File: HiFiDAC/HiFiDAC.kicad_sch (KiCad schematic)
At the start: 16 parts, among them J1 SE, J2 LDIFF, J3 RDIFF, J4 5V, J5 +-15V, U1 KC2520K24.5760

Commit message: HiFiDAC v2 progress
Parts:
- removed C16: 0.1µF C0G, BW_PassiveMechanical:C_0704_1810Metric, symbol Device:C_Small
- removed C2: 1µF 25V, Capacitor_SMD:C_0603_1608Metric, symbol Device:C
- added C1: 10µF 25V, Capacitor_SMD:C_0805_2012Metric, symbol Device:C_Small
- added C10, C11: 0.1µF, Capacitor_SMD:C_0603_1608Metric, symbol Device:C_Small
- added C2, C4, C5, C6: 1µF 25V, Capacitor_SMD:C_0603_1608Metric, symbol Device:C_Small
- added C9: 4.7µF, Capacitor_SMD:C_0603_1608Metric, symbol Device:C_Small
- added FB1: MPZ1608B471ATA00, Inductor_SMD:L_0603_1608Metric, symbol Device:FerriteBead
- added J2: I2S, BW_Connectors:Amphenol_MINITEK_0.8_6P_V, symbol Connector:Conn_01x06_Pin
- added J5: SWD, Connector_PinSocket_1.27mm:PinSocket_1x05_P1.27mm_Vertical_SMD_Pin1Right, symbol Connector:Conn_01x05_Socket
- added J6: I2C, BW_Connectors:Amphenol_MINITEK_0.8_4P_V, symbol Connector:Conn_01x04_Pin
- added R1: 2.2Ω, Resistor_SMD:R_0603_1608Metric, symbol Device:R_US
- added R4, R5: 27Ω, Resistor_SMD:R_0603_1608Metric, symbol Device:R_US
- added R6: 10kΩ, Resistor_SMD:R_0603_1608Metric, symbol Device:R_US
- added TP1: DEBUG_UART_TX, BW_PassiveMechanical:TP_0603_1608Metric_Fused, symbol Connector:TestPoint_Small
- added TP2: I2C_~{INT}, BW_PassiveMechanical:TP_0603_1608Metric_Fused, symbol Connector:TestPoint_Small
- added TP3: I2C_SDA, BW_PassiveMechanical:TP_0603_1608Metric_Fused, symbol Connector:TestPoint_Small
- added TP4: DEBUG_UART_RX, BW_PassiveMechanical:TP_0603_1608Metric_Fused, symbol Connector:TestPoint_Small
- added TP5: I2C_SCL, BW_PassiveMechanical:TP_0603_1608Metric_Fused, symbol Connector:TestPoint_Small
- added U2: ES9039Q2M, BW_Active:QFN-32-1EP_5x5mm_P0.5mm_EP3.2x3.2mm, symbol BW_Active:ES9039Q2M
- added U3: STM32C031K6Ux, Package_DFN_QFN:QFN-32-1EP_5x5mm_P0.5mm_EP3.45x3.45mm, symbol MCU_ST_STM32C0:STM32C031K6Ux
- C12: renamed from C14; value 47µF 20V -> 100µF 25V; footprint Capacitor_SMD:CP_Elec_5x5.8 -> Capacitor_SMD:CP_Elec_6.3x5.9
- C13: renamed from C4; value 100µF 10V 450mΩ -> 100µF 10V; footprint Capacitor_SMD:CP_Elec_6.3x7.7 -> Capacitor_THT:CP_Radial_D6.3mm_P2.50mm
- C14: renamed from C17; value 47µF 20V -> 100µF 25V; footprint Capacitor_SMD:CP_Elec_5x5.8 -> Capacitor_SMD:CP_Elec_6.3x5.9
- C3: value 0.1µF C0G -> 1µF 25V; footprint BW_PassiveMechanical:C_0704_1810Metric -> Capacitor_SMD:C_0603_1608Metric
- J3: renamed from J2; value LDIFF -> DIFF_1
- J4: renamed from J3; value RDIFF -> DIFF_2
- R3: value 0Ω -> 10Ω
- renumbered C12 to C7, C13 to C8, J4 to J7, J5 to J8, R4 to R2
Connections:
- net +3.3VD: now also C10.2, C9.2, FB1.1, J5.1 (Pin_1), R6.1, U3.4 (VDD)
- net GND: now also C10.1, C11.2, C2.2, C4.2, C5.2, C6.2, C9.1, J2.6 (Pin_6), J5.3 (Pin_3), J6.4 (Pin_4), R1.1, U2.11 (GND), U2.17 (RT1), U2.30 (GND), U2.33 (EP), U2.4 (AGND_DAC1), U2.5 (AGND_DAC2), U3.33 (VSS), U3.5 (VSS)
- net at R2.2, U1.3 (CLK): now also U2.32 (MCLK); no longer R3.1
- net at R3.2: now also U2.12 (DATA_CLK)
- net +3.3V: no longer names the net of C3.1
- net +3.3V: now also U2.9 (DVDD)
- net Digital Interface/SCK: no longer names the net of R2.1
- net Digital Interface/SCK: now also J2.5 (Pin_5)
- net I-V Stage/VL+ renamed I-V Stage/V1+
- net I-V Stage/VL- renamed I-V Stage/V1-
- net I-V Stage/VR+ renamed I-V Stage/V2+
- net I-V Stage/VR- renamed I-V Stage/V2-
- new net: J6.2 (Pin_2), TP3.1, U3.31 (PB7)
- new net: C1.1, C2.1, FB1.2, U2.10 (AVDD), U2.29 (MODE)
- new net: R4.2, U2.13 (DATA1)
- new net: R5.2, U2.14 (DATA2)
- new net: U2.15 (SCLK/SCL/HW1), U3.8 (PA1)
- new net: U2.16 (MOSI/SDA/HW0), U3.9 (PA2)
- new net: U2.18 (CHIP_EN), U3.10 (PA3)
- new net: U2.19 (SS/ADDR1/HW2), U3.11 (PA4)
- new net: U2.20 (MISO/ADDR0/MUTE_CTRL), U3.13 (PA6)
- new net: U2.21 (GPIO1), U3.14 (PA7)
- new net: U2.25 (GPIO5), U3.18 (PA8)
- new net: U2.26 (GPIO6), U3.19 (PA9/NC)
- new net: C1.2, R1.2
- new net: C11.1, J5.5 (Pin_5), R6.2, U3.6 (PF2)
- new net: J6.1 (Pin_1), TP5.1, U3.30 (PB6)
- new net: TP4.1, U3.21 (PA10/NC)
- new net: TP1.1, U3.2 (PC14)
- new net: J6.3 (Pin_3), TP2.1, U3.32 (PB8)
- new net 3.3V Supply/3.3VA: C4.1, U2.31 (VCCA)
- new net 3.3V Supply/3.3VDAC1: C5.1, U2.1 (AVCC_DAC1)
- new net 3.3V Supply/3.3VDAC2: C6.1, U2.8 (AVCC_DAC2)
- new net BCK: J2.2 (Pin_2), R3.1
- new net DATA: J2.4 (Pin_4), R5.1
- new net GPIO2: U2.22 (GPIO2), U3.15 (PB0)
- new net GPIO3: U2.23 (GPIO3), U3.16 (PB1)
- new net GPIO4: U2.24 (GPIO4), U3.17 (PB2)
- new net GPIO7: U2.27 (GPIO7), U3.20 (PC6)
- new net I-V Stage/I1+: U2.3 (DAC1)
- new net I-V Stage/I1-: U2.2 (DAC1B)
- new net I-V Stage/I2+: U2.7 (DAC2)
- new net I-V Stage/I2-: U2.6 (DAC2B)
- new net LRCK: J2.3 (Pin_3), R4.1
- new net SWCLK: J5.2 (Pin_2), U3.25 (PA14)
- new net SWDIO: J5.4 (Pin_4), U3.24 (PA13)
- no-connect marks 0 -> 11
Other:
- removed sheet Digital Interface
- sheet 3.3V Supply ports: added 3.3VA, 3.3VD, 3.3VDAC1, 3.3VDAC2; removed 3.3V
- sheet I-V Stage ports: added I1+, I1-, I2+, I2-, V1+, V1-, V2+, V2-; removed IL+, IL-, IR+, IR-, VL+, VL-, VR+, VR-
- moved on the sheet: C7, C8, J1, J3, J4, R2, U1

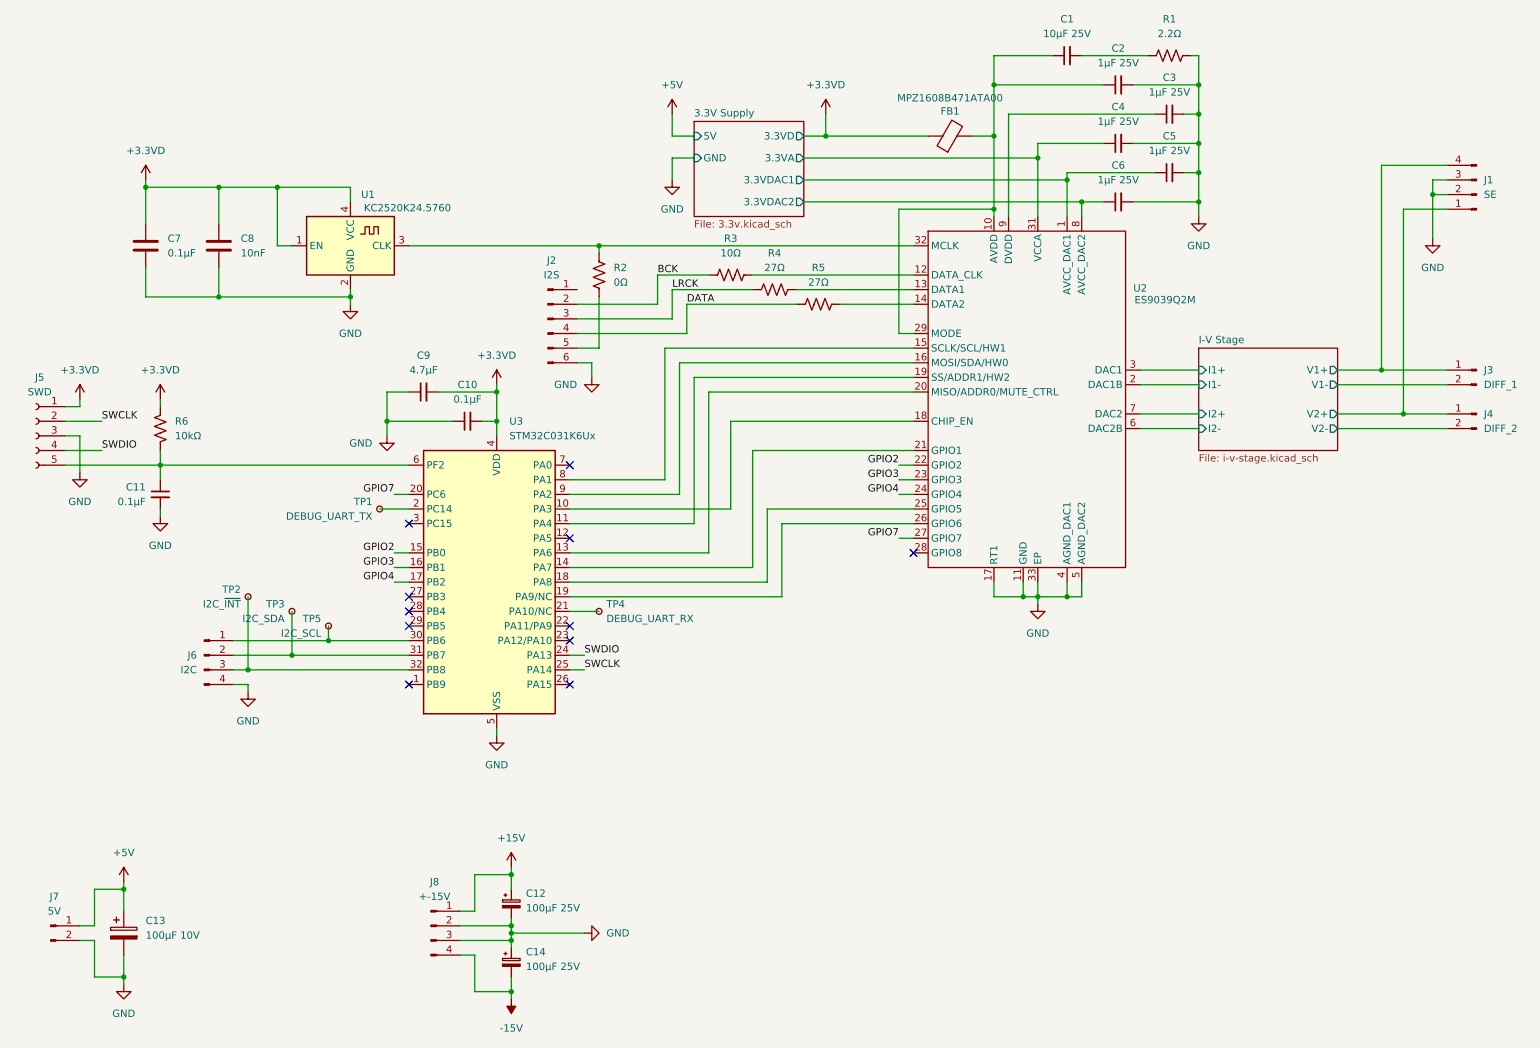
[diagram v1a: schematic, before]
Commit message: HiFiDAC v2 layout+route progress
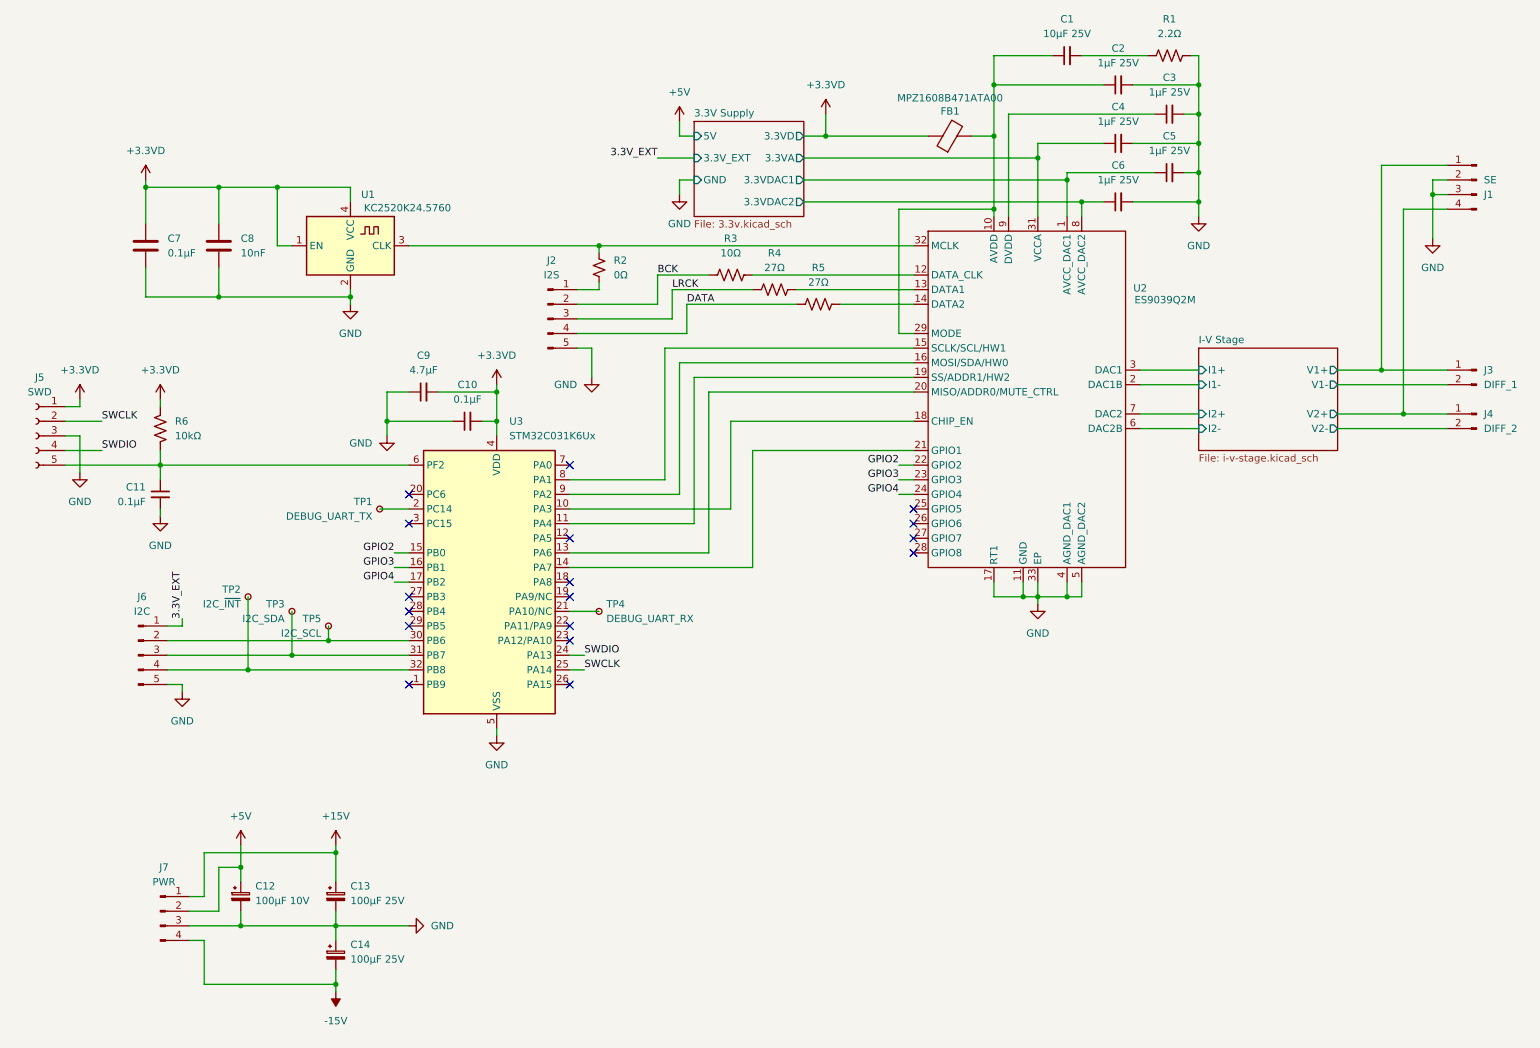
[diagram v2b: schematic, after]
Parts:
- removed J7: 5V, BW_Connectors:Amphenol_MINITEK_0.8_2P_V, symbol Connector:Conn_01x02_Pin
- C12: renamed from C13; symbol Device:C_Polarized -> Device:C_Polarized_Small
- J2: footprint BW_Connectors:Amphenol_MINITEK_0.8_6P_V -> BW_Connectors:Amphenol_MINITEK_WTB_1.25_5P_V; symbol Connector:Conn_01x06_Pin -> Connector:Conn_01x05_Pin
- J6: footprint BW_Connectors:Amphenol_MINITEK_0.8_4P_V -> BW_Connectors:Amphenol_MINITEK_WTB_1.25_5P_V; symbol Connector:Conn_01x04_Pin -> Connector:Conn_01x05_Pin
- J7: renamed from J8; value +-15V -> PWR; footprint BW_Connectors:Amphenol_MINITEK_0.8_4P_V -> BW_Connectors:Amphenol_MINITEK_WTB_1.25_4P_V
- R2: symbol Device:R_US -> Device:R_Small_US
- renumbered C12 to C13
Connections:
- net +5V: now also J7.2 (Pin_2)
- net GND: now also J2.5 (Pin_5), J6.5 (Pin_5); no longer J2.6 (Pin_6), J6.4 (Pin_4), J7.2 (Pin_2)
- net I-V Stage/V1+: now also J1.1 (Pin_1); no longer J1.4 (Pin_4)
- net I-V Stage/V2+: now also J1.4 (Pin_4); no longer J1.1 (Pin_1)
- net at TP3.1, U3.31 (PB7): now also J6.3 (Pin_3); no longer J6.2 (Pin_2)
- net at R2.1: now also J2.1 (Pin_1); no longer J2.5 (Pin_5)
- net at U2.25 (GPIO5): no longer U3.18 (PA8)
- net at U2.26 (GPIO6): no longer U3.19 (PA9/NC)
- net at TP5.1, U3.30 (PB6): now also J6.2 (Pin_2); no longer J6.1 (Pin_1)
- net at TP2.1, U3.32 (PB8): now also J6.4 (Pin_4); no longer J6.3 (Pin_3)
- net GPIO7: no longer names the net of U2.27 (GPIO7)
- net GPIO7: no longer U3.20 (PC6)
- new net 3.3V_EXT: J6.1 (Pin_1)
- no-connect marks 11 -> 17
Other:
- sheet 3.3V Supply ports: added 3.3V_EXT; removed none
- moved on the sheet: C12, C13, C14, J1, J7

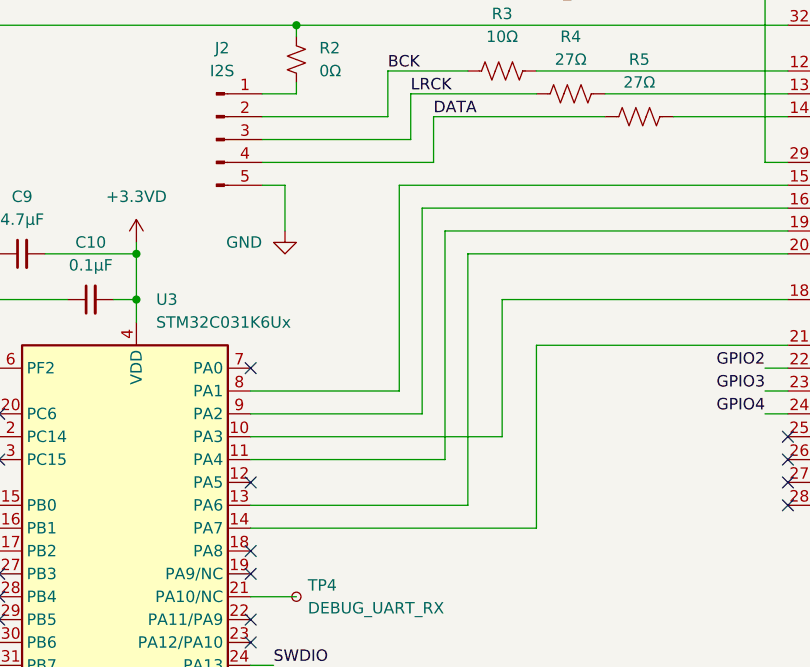
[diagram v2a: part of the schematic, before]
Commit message: HiFiDAC v2 ordered version
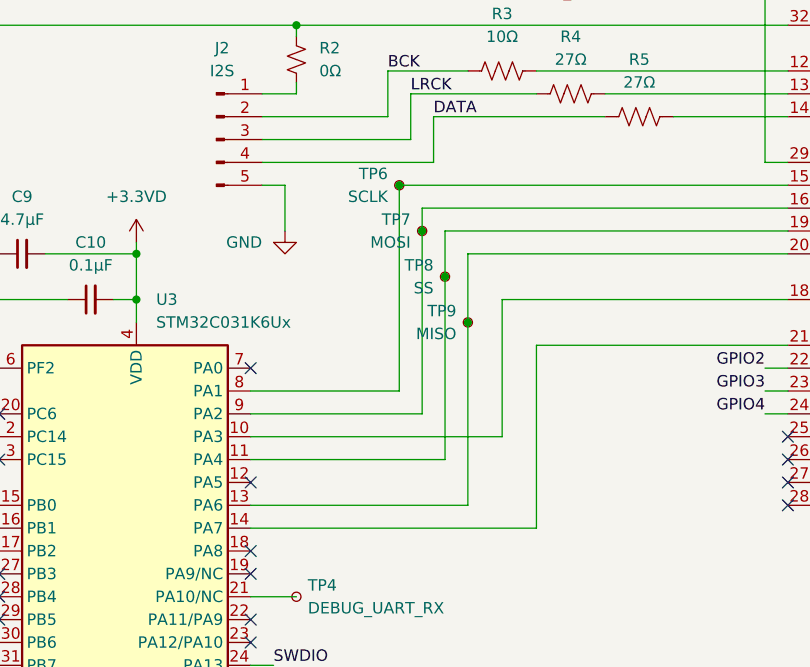
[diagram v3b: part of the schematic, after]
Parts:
- added TP6: SCLK, BW_PassiveMechanical:TP_0603_1608Metric_Fused, symbol Connector:TestPoint_Small
- added TP7: MOSI, BW_PassiveMechanical:TP_0603_1608Metric_Fused, symbol Connector:TestPoint_Small
- added TP8: SS, BW_PassiveMechanical:TP_0603_1608Metric_Fused, symbol Connector:TestPoint_Small
- added TP9: MISO, BW_PassiveMechanical:TP_0603_1608Metric_Fused, symbol Connector:TestPoint_Small
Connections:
- net at U2.15 (SCLK/SCL/HW1), U3.8 (PA1): now also TP6.1
- net at U2.16 (MOSI/SDA/HW0), U3.9 (PA2): now also TP7.1
- net at U2.19 (SS/ADDR1/HW2), U3.11 (PA4): now also TP8.1
- net at U2.20 (MISO/ADDR0/MUTE_CTRL), U3.13 (PA6): now also TP9.1
